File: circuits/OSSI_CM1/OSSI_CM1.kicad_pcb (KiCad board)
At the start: 4 copper layers, 49.5 x 54.9 mm, 73 parts, among them U102 KV30F_64LQFP, U103 LM75B, U104 OPA2317, X101 PINHEADER_2×5, X201 Conn_01x20_Pin, X202 Conn_01x21_Pin, Y101 10MHz

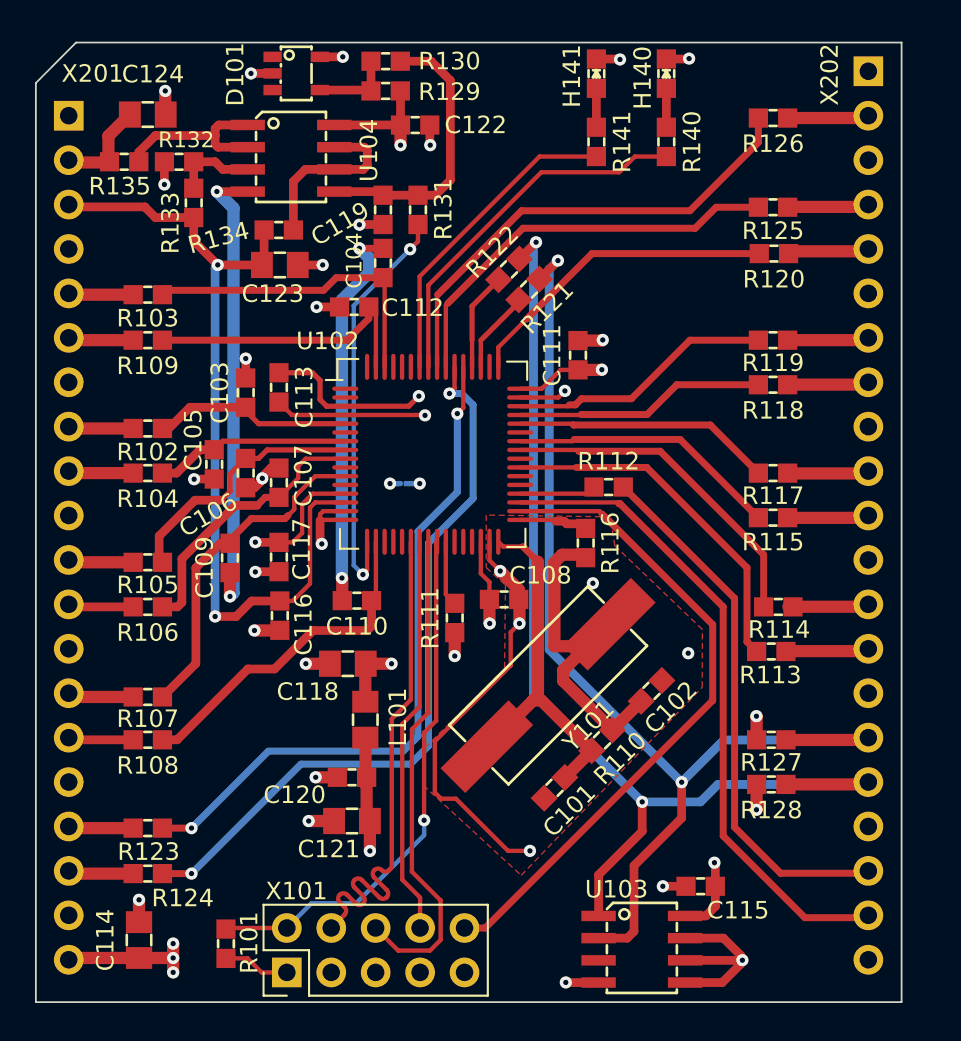
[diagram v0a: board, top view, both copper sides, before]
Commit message: Updates footprint paths
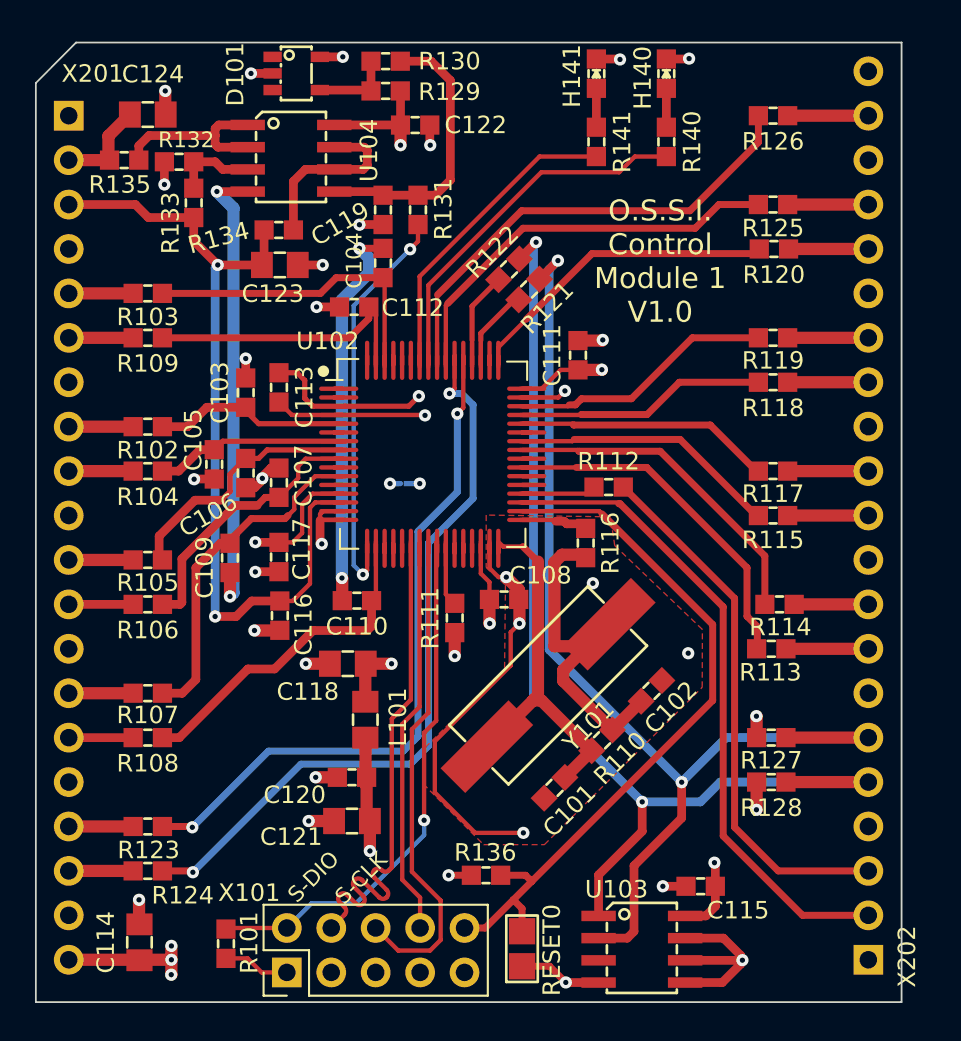
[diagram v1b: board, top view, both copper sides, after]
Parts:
- added R136: 10k, OSSI_standard_footprints:0603_W, F.Cu at (143.2, 120.9)
- added RESET0: Solder_bridge_open, OSSI_standard_footprints:JUMPER_OPEN, F.Cu at (145.3, 125.1)
- moved X202 50.8 mm to (165.1, 125.7), turned to 0 degrees
- moved R120 0.26 mm to (159.7, 85.1)
- moved R107 0.21 mm to (123.9, 110.5)
- moved R114 0.16 mm to (160.0, 105.4)
- moved R113 0.15 mm to (159.6, 108.0)
- moved R124 0.15 mm to (123.9, 120.7)
- moved R125 0.15 mm to (159.7, 82.5)
- moved R106 0.14 mm to (123.9, 105.4)
- moved R118 0.14 mm to (159.7, 92.7)
- moved R105 0.13 mm to (123.9, 102.9)
- moved R109 0.13 mm to (123.9, 90.2)
- moved R119 0.13 mm to (159.7, 90.2)
- moved R126 0.13 mm to (159.7, 77.5)
- moved R128 0.13 mm to (159.6, 115.6)
- moved C114 0.13 mm to (123.4, 124.7)
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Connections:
- net Net-(U102B-~{RESET}) renamed /~{RESET}
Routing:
- net /~{RESET}: track 37.6 -> 41.5 mm
- net GND: track 57.9 -> 60.4 mm
- net +3V3: track 46.5 -> 47.6 mm, vias 11 -> 12
- net I2C_Clk: track 62.1 -> 63.0 mm
- net I2C_Dat: track 60.8 -> 61.7 mm
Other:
- board text added: "O.S.S.I. Control Module 1 V1.0"
- board text added: "S-CLK"
- board text added: "S-DIO"
